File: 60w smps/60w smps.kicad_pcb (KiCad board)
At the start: 2 copper layers, 164 x 61.5 mm, 37 parts, among them J1 Screw_Terminal_01x02, J2 Screw_Terminal_01x02, Q1 2N7000, T1 Transformer_1P_1S, U1 UC3842_DIP8

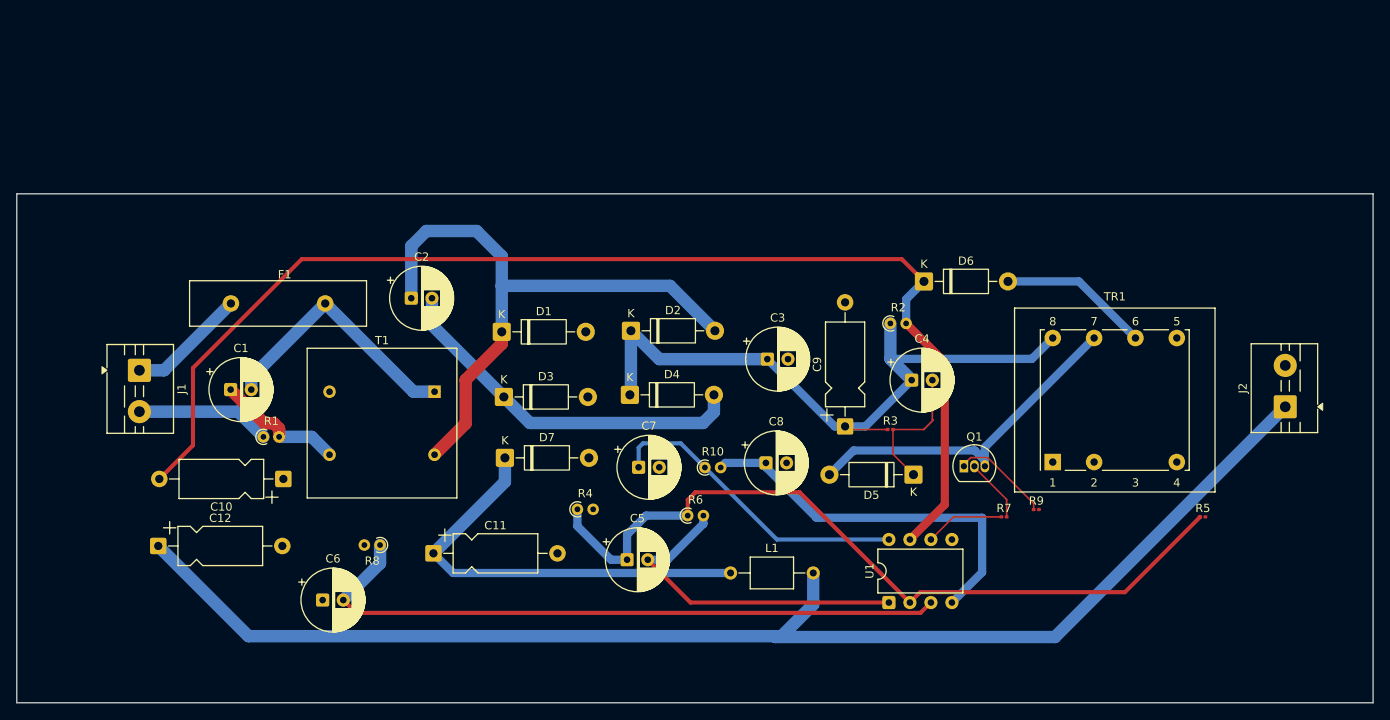
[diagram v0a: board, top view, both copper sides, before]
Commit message: untrack .history pointers and lock files, add new projects
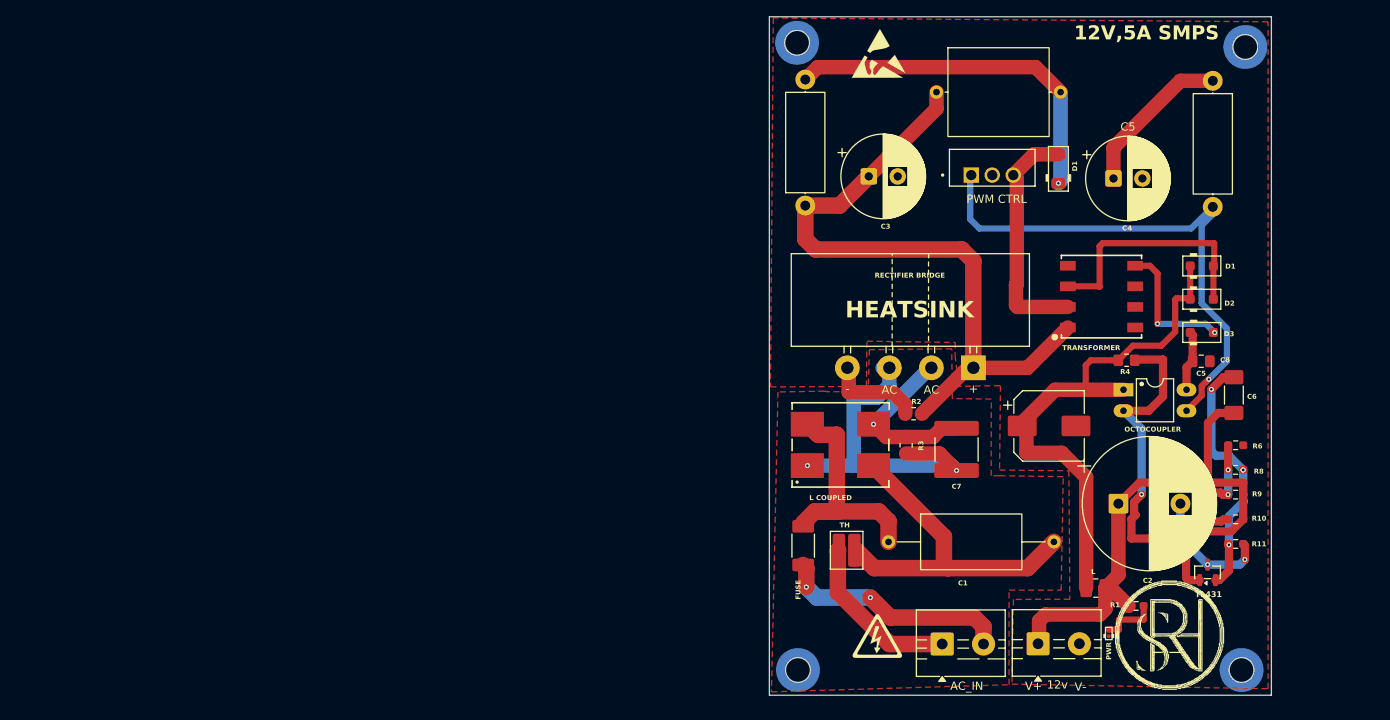
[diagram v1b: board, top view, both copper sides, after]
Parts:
- removed C10, C11, C12: C_Polarized_US, Capacitor_THT:CP_Axial_L10.0mm_D4.5mm_P15.00mm_Horizontal
- removed D1, D7: 1N4007, Diode_THT:D_DO-41_SOD81_P10.16mm_Horizontal
- removed F1: 1A, Fuse:Fuse_Littelfuse-LVR125
- removed J1, J2: Screw_Terminal_01x02, TerminalBlock:TerminalBlock_MaiXu_MX126-5.0-02P_1x02_P5.00mm
- removed Q1: 2N7000, Package_TO_SOT_THT:TO-92_Inline
- removed T1: Transformer_1P_1S, Transformer_THT:Transformer_NF_ETAL_1-1_P1200
- removed TR1: TEZ0.5-D-2, Transformer_THT:Transformer_Breve_TEZ-22x24
- added AC_IN: Screw_Terminal_01x02, TerminalBlock:TerminalBlock_MaiXu_MX126-5.0-02P_1x02_P5.00mm, F.Cu at (152.6, 124.6)
- added F2: 3A, Fuse:Fuse_2010_5025Metric_Pad1.52x2.65mm_HandSolder, F.Cu at (135.8, 112.7)
- added G***: LOGO, custom icons:R logo 20x13.6, F.Cu at (180.6, 123.7)
- added L2: L_Iron_Coupled, inductor_Coupled:WE-MCRI_1040, F.Cu at (140.3, 100.5)
- added LED1: LED_0201_Green, PCM_LED_SMD_AKL:LED_0201_0603Metric, F.Cu at (172.7, 123.3)
- added OC1: PC817, PCM_Package_DIP_AKL:DIP-4_W7.62mm_LongPads, F.Cu at (174.5, 93.9)
- added R11: 3k, Resistor_SMD:R_0603_1608Metric_Pad0.98x0.95mm_HandSolder, F.Cu at (188.1, 112.5)
- added REF**: ESD-Logo_6.6x6mm_SilkScreen, Symbol:ESD-Logo_6.6x6mm_SilkScreen, F.Cu at (144.9, 53.2)
- added REF**: Mounting_Wuerth_WA-SMSI-M2_H1mm_9774010243, Mounting_Wuerth:Mounting_Wuerth_WA-SMSI-M2_H1mm_9774010243, B.Cu at (189.2, 52.4)
- added REF**: Mounting_Wuerth_WA-SMSI-M2_H1mm_9774010243, Mounting_Wuerth:Mounting_Wuerth_WA-SMSI-M2_H1mm_9774010243, B.Cu at (188.8, 127.8)
- added REF**: Mounting_Wuerth_WA-SMSI-M2_H1mm_9774010243, Mounting_Wuerth:Mounting_Wuerth_WA-SMSI-M2_H1mm_9774010243, B.Cu at (135.1, 127.8)
- added REF**: Mounting_Wuerth_WA-SMSI-M2_H1mm_9774010243, Mounting_Wuerth:Mounting_Wuerth_WA-SMSI-M2_H1mm_9774010243, B.Cu at (135.0, 51.9)
- added T2: Transformer_1P_2S, Transformer:WE-IBTI_EP7_L9.78W9.5H10.54, F.Cu at (171.8, 82.6)
- added TH2: 2,5D11, PCM_Resistor_SMD_AKL:R_0815_2038Metric_Pad1.53x4.00mm_HandSolder, F.Cu at (141.0, 113.3)
- added U2: TL431DBZ, Package_TO_SOT_SMD:SOT-23, F.Cu at (184.7, 116.0)
- added V+: OUT DC 12V, TerminalBlock:TerminalBlock_MaiXu_MX126-5.0-02P_1x02_P5.00mm, F.Cu at (164.2, 124.6)
- added s: LOGO, custom icons:electric_Shock, F.Cu at (144.7, 123.6)
- C1: value C -> 150u; footprint Capacitor_THT:CP_Radial_D7.5mm_P2.50mm -> Capacitor_THT:CP_Radial_D10.0mm_P3.50mm
- C2: value C -> 4n7; footprint Capacitor_THT:CP_Radial_D7.5mm_P2.50mm -> Capacitor_THT:C_Axial_L12.0mm_D10.5mm_P15.00mm_Horizontal
- C3: value C -> 0.1uF; footprint Capacitor_THT:CP_Radial_D7.5mm_P2.50mm -> Capacitor_SMD:C_2220_5750Metric
- C4: value C -> 0.1u; footprint Capacitor_THT:CP_Radial_D7.5mm_P2.50mm -> Capacitor_THT:C_Axial_L12.0mm_D6.5mm_P20.00mm_Horizontal
- C5: value C -> 47uF; footprint Capacitor_THT:CP_Radial_D7.5mm_P2.50mm -> Capacitor_THT:CP_Radial_D10.0mm_P3.50mm
- C6: value C -> 1000u 25V; footprint Capacitor_THT:CP_Radial_D7.5mm_P2.50mm -> Capacitor_SMD:CP_Elec_8x10
- C7: footprint Capacitor_THT:CP_Radial_D7.5mm_P2.50mm -> Capacitor_SMD:C_0805_2012Metric_Pad1.18x1.45mm_HandSolder
- C8: value C -> 100u 25v; footprint Capacitor_THT:CP_Radial_D7.5mm_P2.50mm -> Capacitor_THT:CP_Radial_D16.0mm_P7.50mm
- C9: value C_Polarized_US -> 100nF; footprint Capacitor_THT:CP_Axial_L10.0mm_D4.5mm_P15.00mm_Horizontal -> Capacitor_SMD:C_1808_4520Metric_Pad1.72x2.30mm_HandSolder
- D2: value 1N4007 -> BR151L; footprint Diode_THT:D_DO-41_SOD81_P10.16mm_Horizontal -> PCM_Diode_THT_AKL:Diode_Bridge_28.6x28.6x7.3mm_P5.08mm_Vertical
- D3: value 1N4007 -> BYM07-100; footprint Diode_THT:D_DO-41_SOD81_P10.16mm_Horizontal -> PCM_Diode_SMD_AKL:D_MiniMELF
- D4, D5, D6: value 1N4007 -> CRG03; footprint Diode_THT:D_DO-41_SOD81_P10.16mm_Horizontal -> PCM_Diode_SMD_AKL:D_SOD-123F
- L1: value L_Iron -> L; footprint Inductor_THT:L_Axial_L5.0mm_D3.6mm_P10.00mm_Horizontal_Murata_BL01RN1A2A2 -> Inductor_SMD:L_1008_2520Metric_Pad1.43x2.20mm_HandSolder
- R1: value R -> 680K; footprint Resistor_THT:R_Axial_DIN0204_L3.6mm_D1.6mm_P1.90mm_Vertical -> Resistor_SMD:R_0805_2012Metric_Pad1.20x1.40mm_HandSolder
- R10, R8: value R -> 4k7; footprint Resistor_THT:R_Axial_DIN0204_L3.6mm_D1.6mm_P1.90mm_Vertical -> Resistor_SMD:R_0603_1608Metric_Pad0.98x0.95mm_HandSolder
- R2: value R -> 330k; footprint Resistor_THT:R_Axial_DIN0204_L3.6mm_D1.6mm_P1.90mm_Vertical -> Resistor_SMD:R_0805_2012Metric_Pad1.20x1.40mm_HandSolder
- R3: value R -> 47k; footprint Resistor_SMD:R_0201_0603Metric -> Resistor_THT:R_Axial_DIN0414_L11.9mm_D4.5mm_P15.24mm_Horizontal
- R4: value R -> 47k; footprint Resistor_THT:R_Axial_DIN0204_L3.6mm_D1.6mm_P1.90mm_Vertical -> Resistor_THT:R_Axial_DIN0414_L11.9mm_D4.5mm_P15.24mm_Horizontal
- R5: value R -> 2k2; footprint Resistor_SMD:R_0201_0603Metric -> Resistor_SMD:R_0805_2012Metric_Pad1.20x1.40mm_HandSolder
- R6: value R -> 3k3; footprint Resistor_THT:R_Axial_DIN0204_L3.6mm_D1.6mm_P1.90mm_Vertical -> Resistor_SMD:R_0603_1608Metric_Pad0.98x0.95mm_HandSolder
- R7, R9: value R -> 4k7; footprint Resistor_SMD:R_0201_0603Metric -> Resistor_SMD:R_0603_1608Metric_Pad0.98x0.95mm_HandSolder
- U1: value UC3842_DIP8 -> TOP227YN; footprint Package_DIP:DIP-8_W7.62mm -> TOP227YN:TO254P1035X444X2115-3N
- moved R8 103.9 mm to (188.1, 103.6), turned to 0 degrees
- moved R4 92.7 mm to (185.3, 56.5), turned to -90 degrees
- moved C6 90.3 mm to (165.5, 98.2)
- moved C1 81.4 mm to (143.7, 68.1)
- moved R1 78.7 mm to (149.1, 96.8)
- moved C5 74.7 mm to (173.3, 68.3)
- moved D3 72.5 mm to (166.6, 67.2), turned to 90 degrees
- moved D4 70.9 mm to (184.0, 78.9)
- moved C7 69.2 mm to (183.9, 90.4), turned to 180 degrees
- moved C2 68.2 mm to (151.9, 57.9)
- moved R6 66.8 mm to (188.1, 100.6)
- moved R10 64.5 mm to (188.1, 109.5)
- moved U1 54.0 mm to (158.6, 67.0), turned to 0 degrees
- moved C9 47.2 mm to (187.8, 94.5)
- moved L1 44.2 mm to (171.1, 117.9)
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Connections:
- C1 pad 1: Net-(T1-SB) -> /INPUT & RECTIFICATION/DC_IN
- C1 pad 2: Net-(T1-AA) -> GND
- C2 pad 1: Net-(D1-K) -> /INPUT & RECTIFICATION/DC_IN
- C3 pad 1: Net-(D2-K) -> Net-(D2-1)
- C3 pad 2: GND -> Net-(D2-2)
- C4 pad 1: Net-(D2-K) -> Net-(C4-Pad1)
- C4 pad 2: Net-(D5-K) -> Net-(C4-Pad2)
- C5 pad 1: Net-(U1-FB) -> Net-(C5-Pad1)
- C5 pad 2: Net-(U1-COMP) -> GND
- C6 pad 1: GND -> /OUTPUT FILTERING & REGULATION/L2
- C6 pad 2: Net-(U1-CS) -> GND
- C7 pad 1: Net-(U1-VREF) -> GND
- C7 pad 2: GND -> Net-(D6-K)
- C8 pad 1: Net-(U1-RC) -> Net-(J2-Pin_1)
- C9 pad 1: Net-(D2-K) -> Net-(U2-K)
- C9 pad 2: GND -> Net-(U2-REF)
- D2 pad 1: Net-(D2-K) -> /INPUT & RECTIFICATION/DC_IN
- D2 pad 2: Net-(D1-K) -> Net-(D2-1)
- D3 pad 2: GND -> /PWM CONTROLLER n DRIVER/N2
- D4 pad 1: Net-(D2-K) -> /OUTPUT FILTERING & REGULATION/L2
- D4 pad 2: Net-(D3-K) -> Net-(D4-A)
- D5 pad 1: Net-(D5-K) -> /OUTPUT FILTERING & REGULATION/L2
- D5 pad 2: /Q1 -> Net-(D4-A)
- D6 pad 1: /R2 -> Net-(D6-K)
- D6 pad 2: /t6 -> Net-(D6-A)
- L1 pad 1: Net-(D7-K) -> /OUTPUT FILTERING & REGULATION/L2
- L1 pad 2: /DC+ -> Net-(J2-Pin_1)
- R1 pad 1: /220v AC -> GND
- R1 pad 2: Net-(T1-SB) -> /INPUT & RECTIFICATION/DC_IN
- R10 pad 1: Net-(U1-VREF) -> /OUTPUT FILTERING & REGULATION/R7
- R10 pad 2: Net-(U1-RC) -> Net-(U2-K)
- R2 pad 1: Net-(D2-K) -> Net-(D2-1)
- R2 pad 2: /R2 -> Net-(D2-2)
- R3 pad 1: Net-(D2-K) -> /INPUT & RECTIFICATION/DC_IN
- R3 pad 2: Net-(D5-K) -> Net-(D3-K)
- R4 pad 1: Net-(U1-FB) -> Net-(C5-Pad1)
- R4 pad 2: GND -> /PWM CONTROLLER n DRIVER/CTRL
- R5 pad 1: Net-(U1-FB) -> /OUTPUT FILTERING & REGULATION/L2
- R5 pad 2: /R2 -> /OUTPUT FILTERING & REGULATION/R7
- R6 pad 1: Net-(U1-FB) -> Net-(J2-Pin_1)
- R6 pad 2: Net-(U1-COMP) -> GND
- R7 pad 1: Net-(U1-OUT) -> Net-(J2-Pin_1)
- R8 pad 1: Net-(U1-CS) -> Net-(J2-Pin_1)
- R8 pad 2: Net-(Q1-S) -> Net-(U2-REF)
- R9 pad 1: Net-(Q1-S) -> Net-(J2-Pin_1)
- R9 pad 2: GND -> Net-(U2-K)
- U1 pad 1: Net-(U1-COMP) -> /PWM CONTROLLER n DRIVER/CTRL
- U1 pad 2: Net-(U1-FB) -> GND
- U1 pad 3: Net-(U1-CS) -> /PWM CONTROLLER n DRIVER/N2
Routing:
- net /DC+: track 162.4 -> 0.00 mm
- net /R2: track 145.9 -> 0.00 mm
- net Net-(U1-FB): track 95.1 -> 0.00 mm
- net /INPUT & RECTIFICATION/DC_IN: track 0.00 -> 83.1 mm
- net Net-(D2-K): track 82.8 -> 0.00 mm
- net Net-(U1-CS): track 80.7 -> 0.00 mm
- net Net-(D1-K): track 74.7 -> 0.00 mm
- net /OUTPUT FILTERING & REGULATION/L2: track 0.00 -> 65.0 mm
- net /PWM CONTROLLER n DRIVER/CTRL: track 0.00 -> 64.8 mm, vias 0 -> 1
- net Net-(D7-K): track 52.0 -> 0.00 mm
- net Net-(J2-Pin_1): track 0.00 -> 49.4 mm, vias 0 -> 2
- net Net-(U1-RC): track 46.7 -> 0.00 mm
- net /OUTPUT FILTERING & REGULATION/R7: track 0.00 -> 43.1 mm, vias 0 -> 1
- net Net-(C4-Pad2): track 0.00 -> 42.2 mm
- net /Q1: track 42.2 -> 0.00 mm
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- added copper zone on F.Cu, net GND
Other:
- board size 164 x 61.5 mm -> 60.7 x 82 mm
- board text added: "12V,5A SMPS"
- board text added: "12v"
- board text added: "C1"
- board text added: "C2"
- board text added: "C3"
- board text added: "C4"
- board text added: "C5"
- board text added: "C6"
- board text added: "C7"
- board text added: "C8"
- board text added: "D1"
- board text added: "D2"
- board text added: "D3"
- board text added: "FUSE"
- board text added: "HEATSINK"
- board text added: "L"
- board text added: "L COUPLED"
- board text added: "OCTOCOUPLER"
- board text added: "PWM CTRL"
- board text added: "PWR"
- board text added: "R1"
- board text added: "R10"
- board text added: "R11"
- board text added: "R2"
- board text added: "R3"
- board text added: "R4"
- board text added: "R6"
- board text added: "R8"
- board text added: "R9"
- board text added: "RECTIFIER BRIDGE"
- board text added: "TH"
- board text added: "TL431"
- board text added: "TRANSFORMER"
- board text added: "V-"
